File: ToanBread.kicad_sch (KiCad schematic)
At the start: 13 parts, among them J1 PJ-059A, J2 AUDIO_IN, J3 VBias_Out, J4 9V_Out, J5 AUDIO_OUT

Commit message: Associate most components
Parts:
- added C2, C6: 10u, Capacitor_THT:CP_Radial_D5.0mm_P2.00mm, symbol Device:C_Polarized
- added C3: 1n, Capacitor_THT:C_Rect_L7.0mm_W2.5mm_P5.00mm, symbol Device:C
- added C4, C5: 100n, Capacitor_THT:C_Rect_L7.0mm_W2.5mm_P5.00mm, symbol Device:C
- added D2: INPUT_BUF, LED_THT:LED_D5.0mm, symbol Device:LED
- added D3: OUTPUT_BUF, LED_THT:LED_D5.0mm, symbol Device:LED
- added J6: EFF_OUT, Connector_PinSocket_2.54mm:PinSocket_1x02_P2.54mm_Vertical, symbol Connector_Generic:Conn_01x02
- added J7: EFF_IN, Connector_PinSocket_2.54mm:PinSocket_1x02_P2.54mm_Vertical, symbol Connector_Generic:Conn_01x02
- added R10, R7: 4.7k, Resistor_THT:R_Axial_DIN0204_L3.6mm_D1.6mm_P5.08mm_Horizontal, symbol Device:R
- added R11, R4, R6, R8: 1M, Resistor_THT:R_Axial_DIN0204_L3.6mm_D1.6mm_P5.08mm_Horizontal, symbol Device:R
- added R5: 1k, Resistor_THT:R_Axial_DIN0204_L3.6mm_D1.6mm_P5.08mm_Horizontal, symbol Device:R
- added S2, S3: GF-126-0159, ProjectSpecific:SW_GF-126-0159, symbol ProjectSpecific:GF-126-0159
- added U1: LM4562NA, ProjectSpecific:DIP794W45P254L959H508Q8, symbol ProjectSpecific:LM4562NA
- BT1, R1: footprint (none) -> Connector_PinSocket_2.54mm:PinSocket_1x02_P2.54mm_Vertical
- C1: footprint (none) -> Capacitor_THT:CP_Radial_D5.0mm_P2.00mm
- D1: footprint (none) -> LED_THT:LED_D5.0mm
- J1: footprint PJ-059A:CUI_PJ-059A -> ProjectSpecific:CUI_PJ-059A
- J2, J5: footprint SJ-63053A:CUI_SJ-63053A -> ProjectSpecific:CUI_SJ-63053A
- J3: value VBias_Out -> VBIAS_OUT; footprint (none) -> Connector_PinSocket_2.54mm:PinSocket_1x02_P2.54mm_Vertical
- J4: value 9V_Out -> 9V_OUT; footprint (none) -> Connector_PinSocket_2.54mm:PinSocket_1x02_P2.54mm_Vertical
- R2, R3: footprint (none) -> Resistor_THT:R_Axial_DIN0204_L3.6mm_D1.6mm_P5.08mm_Horizontal
- S1: footprint FS57003PLT2B2M2QE:SW_FS57003PLT2B2M2QE -> ProjectSpecific:SW_FS57003PLT2B2M2QE
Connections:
- net +9V: now also S2.5, U1.8
- net 4V5: now also R4.1, R8.1
- net BUF1_{IN}: now also R6.1, S2.2
- net BUF2_{OUT}: now also C6.2, R11.2, S3.3
- net GND: now also C3.1, D2.1 (K), D3.1 (K), R11.1, R6.2, U1.4
- net SIG_{IN} renamed SIG
- net V_{BIAS}: no longer names the net of J3.2 (Pin_2), RV1.2
- new net: D3.2 (A), R10.1
- new net: J7.1 (Pin_1), J7.2 (Pin_2), S3.2
- new net: R10.2, S3.4
- new net: R5.1, S2.1
- new net: C2.2, J6.1 (Pin_1), J6.2 (Pin_2), S2.3
- new net: R7.1, S2.4
- new net: C3.2, C4.1, R5.2
- new net: C5.2, R8.2, U1.5
- new net: C6.1, U1.6, U1.7
- new net: C2.1, U1.1, U1.2
- new net: D2.2 (A), R7.2
- new net: C4.2, R4.2, U1.3
- new net: C5.1, S3.1
- no-connect marks 0 -> 2
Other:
- note added: "Input Buffer"
- note added: "Output Buffer"
- moved on the sheet: BT1, C1, D1, J1, J2, J3, J4, J5, R1, R2, R3, RV1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

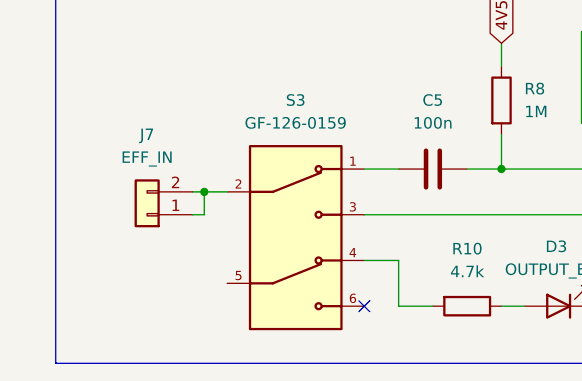
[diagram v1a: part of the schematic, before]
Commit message: Complete initial v0.3 board layout
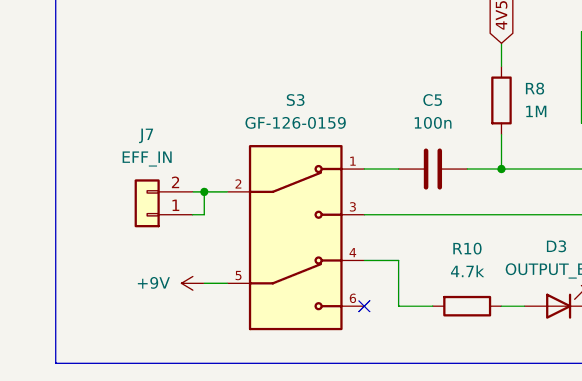
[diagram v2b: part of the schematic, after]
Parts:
- R1: footprint Connector_PinSocket_2.54mm:PinSocket_1x02_P2.54mm_Vertical -> Resistor_THT:R_Axial_DIN0204_L3.6mm_D1.6mm_P5.08mm_Horizontal
- RV1: footprint (none) -> ProjectSpecific:PTN16-A20120K1B1
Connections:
- net +9V: now also S3.5
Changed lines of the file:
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@@
 		)
 	)
+	(wire
+		(pts
+			(xy 38.1 185.42) (xy 40.64 185.42)
+		)
+		(stroke
+			(width 0)
+			(type default)
+		)
+	)
 	(rectangle
 		(start 21.59 90.17)
@@
 			)
 		)
-		(property "Footprint" ""
+		(property "Footprint" "ProjectSpecific:PTN16-A20120K1B1"
 			(at 213.36 134.62 0)
 			(effects
@@
 			)
 		)
-		(property "Footprint" "Connector_PinSocket_2.54mm:PinSocket_1x02_P2.54mm_Vertical"
+		(property "Footprint" "Resistor_THT:R_Axial_DIN0204_L3.6mm_D1.6mm_P5.08mm_Horizontal"
 			(at 207.01 110.998 90)
 			(effects
@@
 					(unit 1)
 				)
+			)
+		)
+	)
+	(symbol
+		(lib_id "power:+9V")
+		(at 38.1 185.42 90)
+		(unit 1)
+		(exclude_from_sim no)
+		(in_bom yes)
+		(on_board yes)
+		(dnp no)
+		(fields_autoplaced yes)
+		(property "Reference" "#PWR016"
+			(at 41.91 185.42 0)
+			(effects
+				(font
+					(size 1.27 1.27)
+				)
+				(hide yes)
+			)
+		)
+		(property "Value" "+9V"
+			(at 34.29 185.4199 90)
+			(effects
+				(font
+					(size 1.27 1.27)
+				)
+				(justify left)
+			)
+		)
+		(property "Footprint" ""
+			(at 38.1 185.42 0)
+			(effects
+				(font
+					(size 1.27 1.27)
+				)
+				(hide yes)
+			)
+		)
+		(property "Datasheet" ""
+			(at 38.1 185.42 0)
+			(effects
+				(font
+					(size 1.27 1.27)
+				)
+				(hide yes)
+			)
+		)
+		(property "Description" "Power symbol creates a global label with name \"+9V\""
+			(at 38.1 185.42 0)
+			(effects
+				(font
+					(size 1.27 1.27)
+				)
+				(hide yes)
+			)
+		)
+		(pin "1"
+		)
+		(instances
+			(project "ToanBread"
+				(path "/d4b15b0c-595c-484d-8838-94bb74644084"
+					(reference "#PWR016")
+					(unit 1)
+				)

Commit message: Add info and logo to silkscreen
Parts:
- BT1, J3, J4, J6, J7: footprint Connector_PinSocket_2.54mm:PinSocket_1x02_P2.54mm_Vertical -> Connector_PinHeader_2.54mm:PinHeader_1x02_P2.54mm_Vertical
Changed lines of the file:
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@@
 			)
 		)
-		(property "Footprint" "Connector_PinSocket_2.54mm:PinSocket_1x02_P2.54mm_Vertical"
+		(property "Footprint" "Connector_PinHeader_2.54mm:PinHeader_1x02_P2.54mm_Vertical"
 			(at 31.75 177.8 0)
 			(effects
@@
 			)
 		)
-		(property "Footprint" "Connector_PinSocket_2.54mm:PinSocket_1x02_P2.54mm_Vertical"
+		(property "Footprint" "Connector_PinHeader_2.54mm:PinHeader_1x02_P2.54mm_Vertical"
 			(at 212.09 91.44 0)
 			(effects
@@
 			)
 		)
-		(property "Footprint" "Connector_PinSocket_2.54mm:PinSocket_1x02_P2.54mm_Vertical"
+		(property "Footprint" "Connector_PinHeader_2.54mm:PinHeader_1x02_P2.54mm_Vertical"
 			(at 71.12 39.116 90)
 			(effects
@@
 			)
 		)
-		(property "Footprint" "Connector_PinSocket_2.54mm:PinSocket_1x02_P2.54mm_Vertical"
+		(property "Footprint" "Connector_PinHeader_2.54mm:PinHeader_1x02_P2.54mm_Vertical"
 			(at 143.51 114.3 0)
 			(effects
@@
 			)
 		)
-		(property "Footprint" "Connector_PinSocket_2.54mm:PinSocket_1x02_P2.54mm_Vertical"
+		(property "Footprint" "Connector_PinHeader_2.54mm:PinHeader_1x02_P2.54mm_Vertical"
 			(at 220.98 149.86 0)
 			(effects

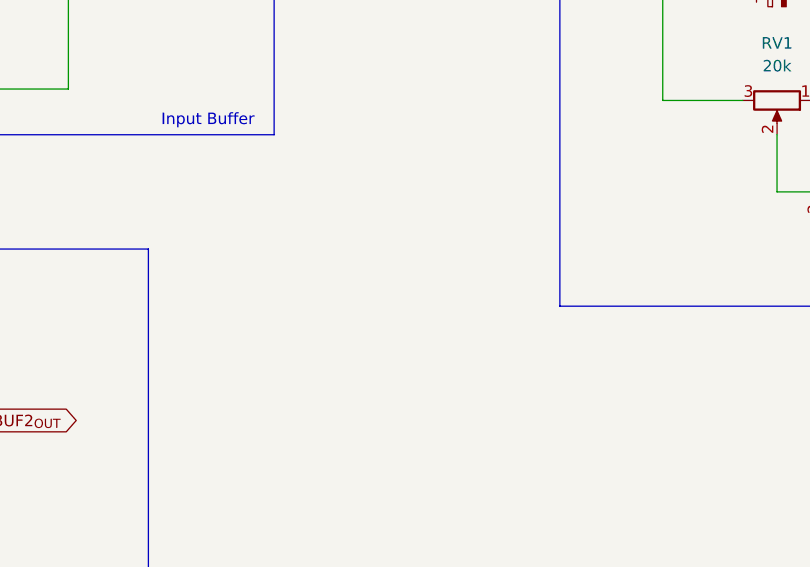
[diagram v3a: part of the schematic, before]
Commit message: Fix resistor footprints
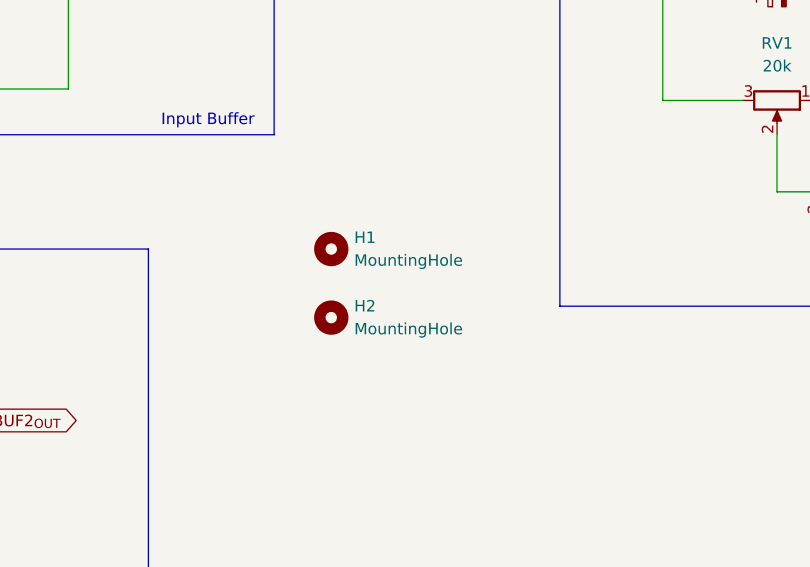
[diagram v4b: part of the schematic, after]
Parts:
- added H1, H2: MountingHole, MountingHole:MountingHole_3.2mm_M3_DIN965, symbol Mechanical:MountingHole
- R1, R10, R11, R2, R3, R4, R5, R6, R7, R8: footprint Resistor_THT:R_Axial_DIN0204_L3.6mm_D1.6mm_P5.08mm_Horizontal -> Resistor_THT:R_Axial_DIN0207_L6.3mm_D2.5mm_P7.62mm_Horizontal
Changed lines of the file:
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@@
 			)
 		)
-		(property "Footprint" "Resistor_THT:R_Axial_DIN0204_L3.6mm_D1.6mm_P5.08mm_Horizontal"
+		(property "Footprint" "Resistor_THT:R_Axial_DIN0207_L6.3mm_D2.5mm_P7.62mm_Horizontal"
 			(at 67.31 186.182 90)
 			(effects
@@
 	)
 	(symbol
+		(lib_id "Mechanical:MountingHole")
+		(at 163.83 158.75 0)
+		(unit 1)
+		(exclude_from_sim yes)
+		(in_bom no)
+		(on_board yes)
+		(dnp no)
+		(fields_autoplaced yes)
+		(property "Reference" "H2"
+			(at 166.37 157.4799 0)
+			(effects
+				(font
+					(size 1.27 1.27)
+				)
+				(justify left)
+			)
+		)
+		(property "Value" "MountingHole"
+			(at 166.37 160.0199 0)
+			(effects
+				(font
+					(size 1.27 1.27)
+				)
+				(justify left)
+			)
+		)
+		(property "Footprint" "MountingHole:MountingHole_3.2mm_M3_DIN965"
+			(at 163.83 158.75 0)
+			(effects
+				(font
+					(size 1.27 1.27)
+				)
+				(hide yes)
+			)
+		)
+		(property "Datasheet" "~"
+			(at 163.83 158.75 0)
+			(effects
+				(font
+					(size 1.27 1.27)
+				)
+				(hide yes)
+			)
+		)
+		(property "Description" "Mounting Hole without connection"
+			(at 163.83 158.75 0)
+			(effects
+				(font
+					(size 1.27 1.27)
+				)
+				(hide yes)
+			)
+		)
+		(instances
+			(project "ToanBread"
+				(path "/d4b15b0c-595c-484d-8838-94bb74644084"
+					(reference "H2")
+					(unit 1)
+				)
+			)
+		)
+	)
+	(symbol
 		(lib_id "Device:R")
 		(at 55.88 116.84 90)
@@
 			)
 		)
-		(property "Footprint" "Resistor_THT:R_Axial_DIN0204_L3.6mm_D1.6mm_P5.08mm_Horizontal"
+		(property "Footprint" "Resistor_THT:R_Axial_DIN0207_L6.3mm_D2.5mm_P7.62mm_Horizontal"
 			(at 55.88 118.618 90)
 			(effects
@@
 			)
 		)
-		(property "Footprint" "Resistor_THT:R_Axial_DIN0204_L3.6mm_D1.6mm_P5.08mm_Horizontal"
+		(property "Footprint" "Resistor_THT:R_Axial_DIN0207_L6.3mm_D2.5mm_P7.62mm_Horizontal"
 			(at 69.342 165.1 90)
 			(effects
@@
 			)
 		)
-		(property "Footprint" "Resistor_THT:R_Axial_DIN0204_L3.6mm_D1.6mm_P5.08mm_Horizontal"
+		(property "Footprint" "Resistor_THT:R_Axial_DIN0207_L6.3mm_D2.5mm_P7.62mm_Horizontal"
 			(at 162.56 67.818 90)
 			(effects
@@
 			)
 		)
-		(property "Footprint" "Resistor_THT:R_Axial_DIN0204_L3.6mm_D1.6mm_P5.08mm_Horizontal"
+		(property "Footprint" "Resistor_THT:R_Axial_DIN0207_L6.3mm_D2.5mm_P7.62mm_Horizontal"
 			(at 188.722 54.61 90)
 			(effects
@@
 			)
 		)
-		(property "Footprint" "Resistor_THT:R_Axial_DIN0204_L3.6mm_D1.6mm_P5.08mm_Horizontal"
+		(property "Footprint" "Resistor_THT:R_Axial_DIN0207_L6.3mm_D2.5mm_P7.62mm_Horizontal"
 			(at 207.01 110.998 90)
 			(effects
@@
 			)
 		)
-		(property "Footprint" "Resistor_THT:R_Axial_DIN0204_L3.6mm_D1.6mm_P5.08mm_Horizontal"
+		(property "Footprint" "Resistor_THT:R_Axial_DIN0207_L6.3mm_D2.5mm_P7.62mm_Horizontal"
 			(at 219.71 110.998 90)
 			(effects
@@
 	)
 	(symbol
+		(lib_id "Mechanical:MountingHole")
+		(at 163.83 151.13 0)
+		(unit 1)
+		(exclude_from_sim yes)
+		(in_bom no)
+		(on_board yes)
+		(dnp no)
+		(fields_autoplaced yes)
+		(property "Reference" "H1"
+			(at 166.37 149.8599 0)
+			(effects
+				(font
+					(size 1.27 1.27)
+				)
+				(justify left)
+			)
+		)
+		(property "Value" "MountingHole"
+			(at 166.37 152.3999 0)
+			(effects
+				(font
+					(size 1.27 1.27)
+				)
+				(justify left)
+			)
+		)
+		(property "Footprint" "MountingHole:MountingHole_3.2mm_M3_DIN965"
+			(at 163.83 151.13 0)
+			(effects
+				(font
+					(size 1.27 1.27)
+				)
+				(hide yes)
+			)
+		)
+		(property "Datasheet" "~"
+			(at 163.83 151.13 0)
+			(effects
+				(font
+					(size 1.27 1.27)
+				)
+				(hide yes)
+			)
+		)
+		(property "Description" "Mounting Hole without connection"
+			(at 163.83 151.13 0)
+			(effects
+				(font
+					(size 1.27 1.27)
+				)
+				(hide yes)
+			)
+		)
+		(instances
+			(project "ToanBread"
+				(path "/d4b15b0c-595c-484d-8838-94bb74644084"
+					(reference "H1")
+					(unit 1)
+				)
+			)
+		)
+	)
+	(symbol
 		(lib_id "Device:R")
 		(at 58.42 132.08 90)
@@
 			)
 		)
-		(property "Footprint" "Resistor_THT:R_Axial_DIN0204_L3.6mm_D1.6mm_P5.08mm_Horizontal"
+		(property "Footprint" "Resistor_THT:R_Axial_DIN0207_L6.3mm_D2.5mm_P7.62mm_Horizontal"
 			(at 58.42 133.858 90)
 			(effects
@@
 			)
 		)
-		(property "Footprint" "Resistor_THT:R_Axial_DIN0204_L3.6mm_D1.6mm_P5.08mm_Horizontal"
+		(property "Footprint" "Resistor_THT:R_Axial_DIN0207_L6.3mm_D2.5mm_P7.62mm_Horizontal"
 			(at 130.302 34.29 90)
 			(effects
@@
 			)
 		)
-		(property "Footprint" "Resistor_THT:R_Axial_DIN0204_L3.6mm_D1.6mm_P5.08mm_Horizontal"
+		(property "Footprint" "Resistor_THT:R_Axial_DIN0207_L6.3mm_D2.5mm_P7.62mm_Horizontal"
 			(at 84.582 107.95 90)
 			(effects

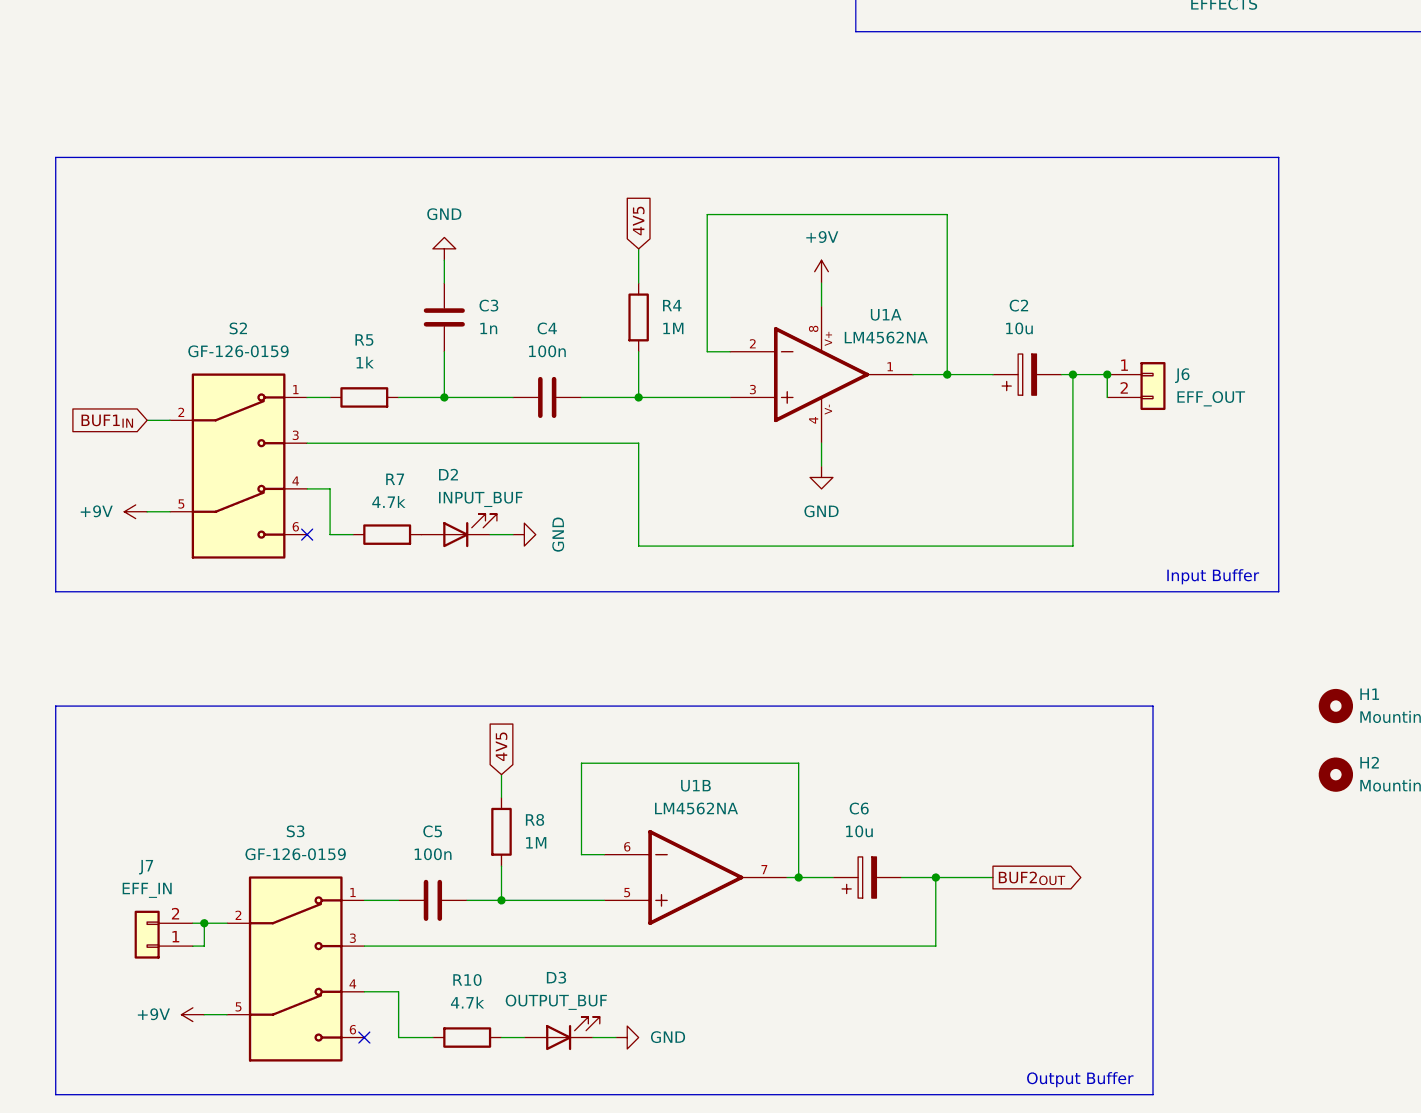
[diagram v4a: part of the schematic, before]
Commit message: Fix input and output buffer switches
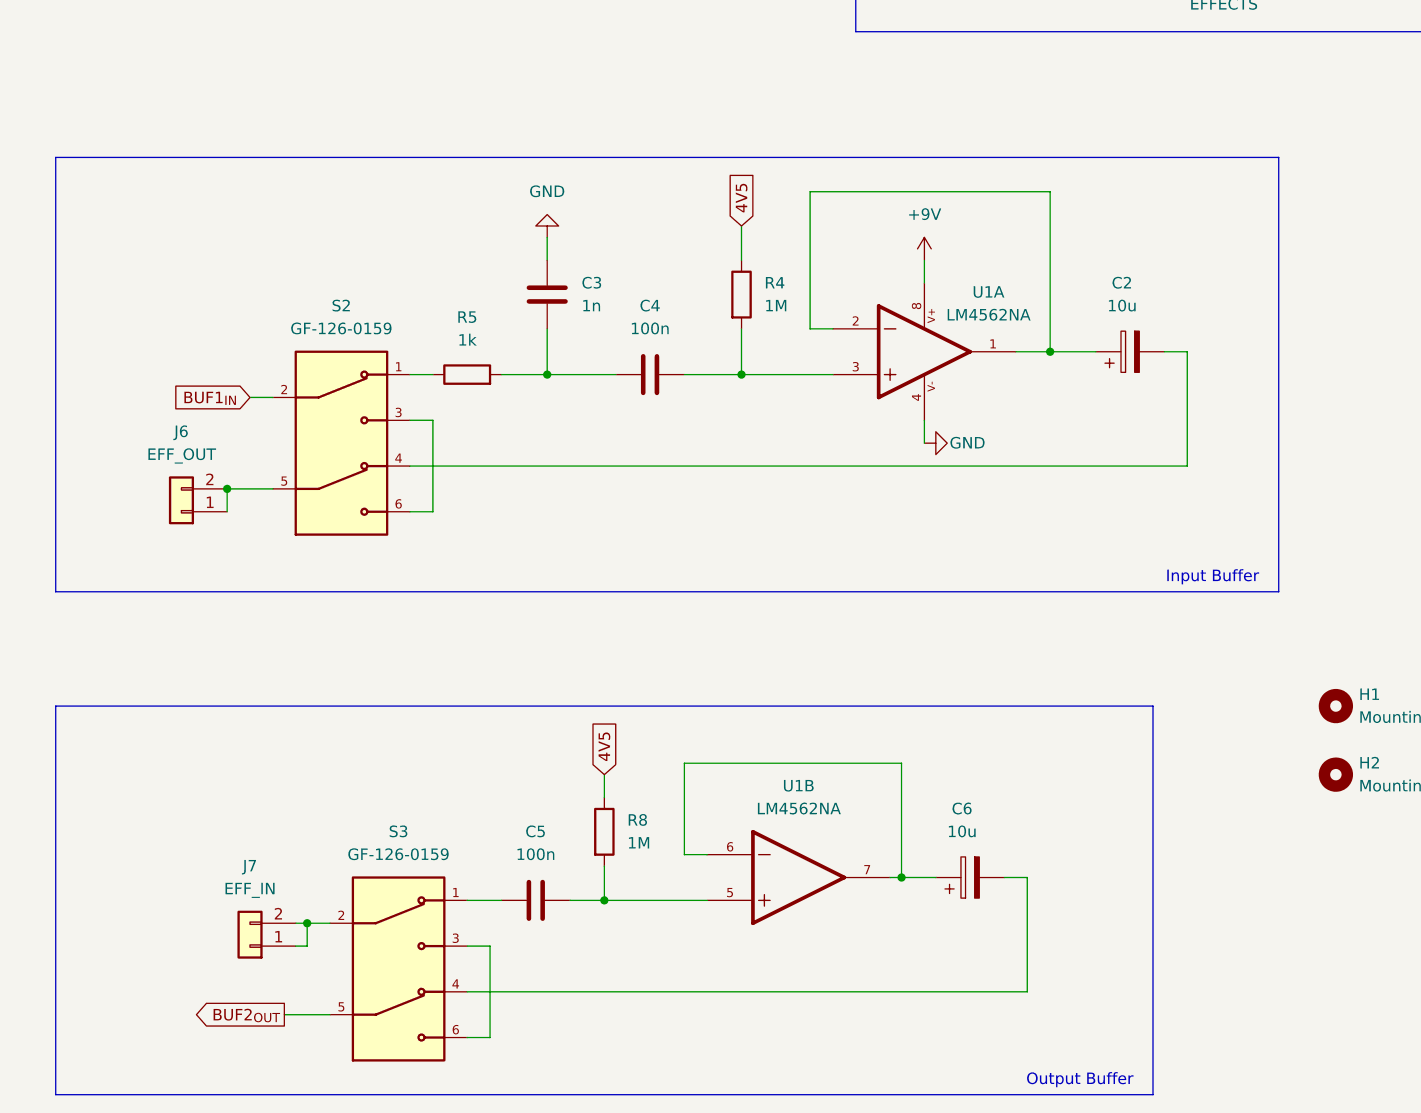
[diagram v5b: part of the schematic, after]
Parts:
- removed D2: INPUT_BUF, LED_THT:LED_D5.0mm, symbol Device:LED
- removed D3: OUTPUT_BUF, LED_THT:LED_D5.0mm, symbol Device:LED
- removed R10, R7: 4.7k, Resistor_THT:R_Axial_DIN0207_L6.3mm_D2.5mm_P7.62mm_Horizontal, symbol Device:R
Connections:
- net +9V: no longer S2.5, S3.5
- net BUF2_{OUT}: now also S3.5; no longer C6.2, S3.3
- net at S3.4: now also C6.2
- net at J6.1 (Pin_1), J6.2 (Pin_2): now also S2.5; no longer C2.2, S2.3
- net at S2.4: now also C2.2
- net at S2.6: now also S2.3
- net at S3.6: now also S3.3
- no-connect marks 2 -> 0
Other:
- moved on the sheet: C2, C3, C4, C5, C6, J6, J7, R4, R5, R8, S2, S3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
